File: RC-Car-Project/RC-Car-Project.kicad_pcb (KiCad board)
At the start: 2 copper layers, 80 x 120 mm, 136 parts, among them J1 Conn_01x02_Pin, J10 ANT_IF, J11 Conn_01x02, J12 Conn_01x02, J2 Conn_01x02_Pin, J3 Conn_01x02_Pin, J4 Conn_01x02_Pin, J5 MCU_IF, J6 Conn_01x02, J7 Conn_01x02, J8 Conn_01x02, J9 Conn_02x09_Odd_Even, Q1 BTN8982TA, Q2 BTN8982TA, Q3 BTN8982TA, Q4 2N7002E, Q4 BTN8982TA, Q5 2N7002E, Q6 2N7002E, Q7 PMOS, SW1 SW_Push, U1 LMR16020PDDAR, U10 2450LP14A0100001T, U2 A6986F3V3TR, U3 STM32H743VGTx, U4 AT86RF215-ZU, U5 2450FB15A050E, U6 RFX2401C, U7 INA229AQDGSRQ1, U8 ADC082S021CIMM/NOPB, U9 SN74HC244PWR, Y1 Crystal

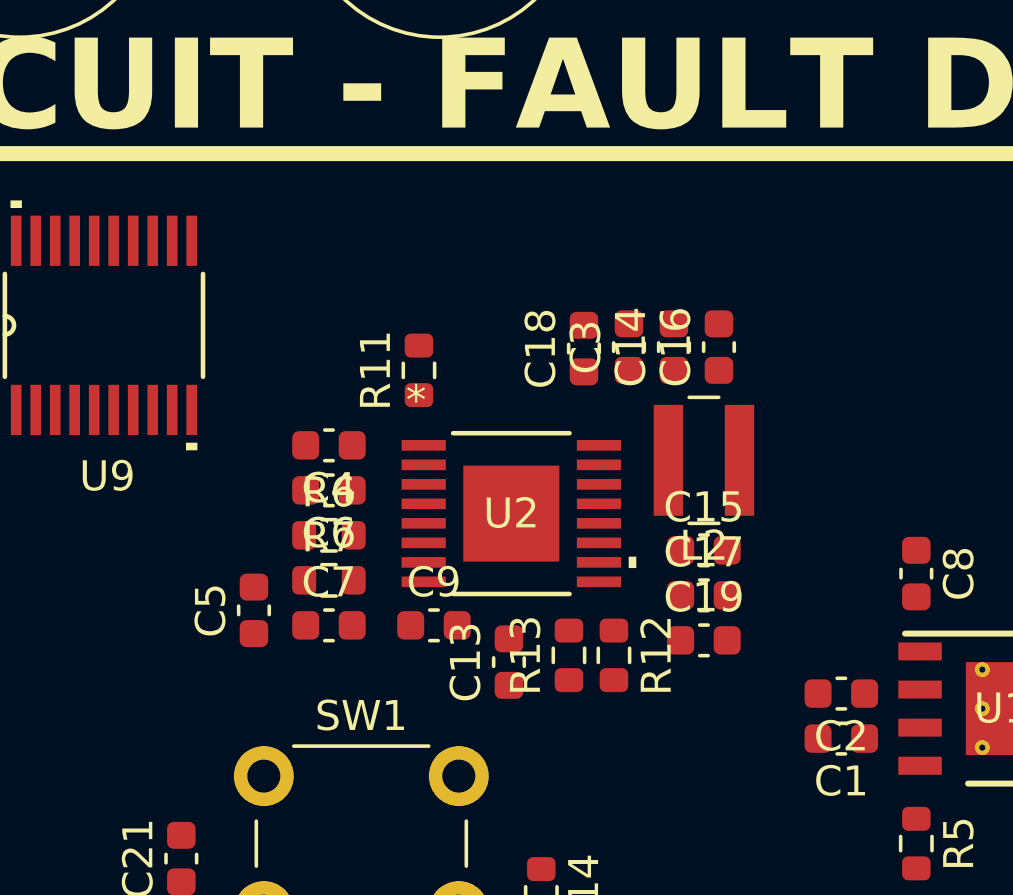
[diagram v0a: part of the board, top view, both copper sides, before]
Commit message: Update DC power supply to 3A and 60V
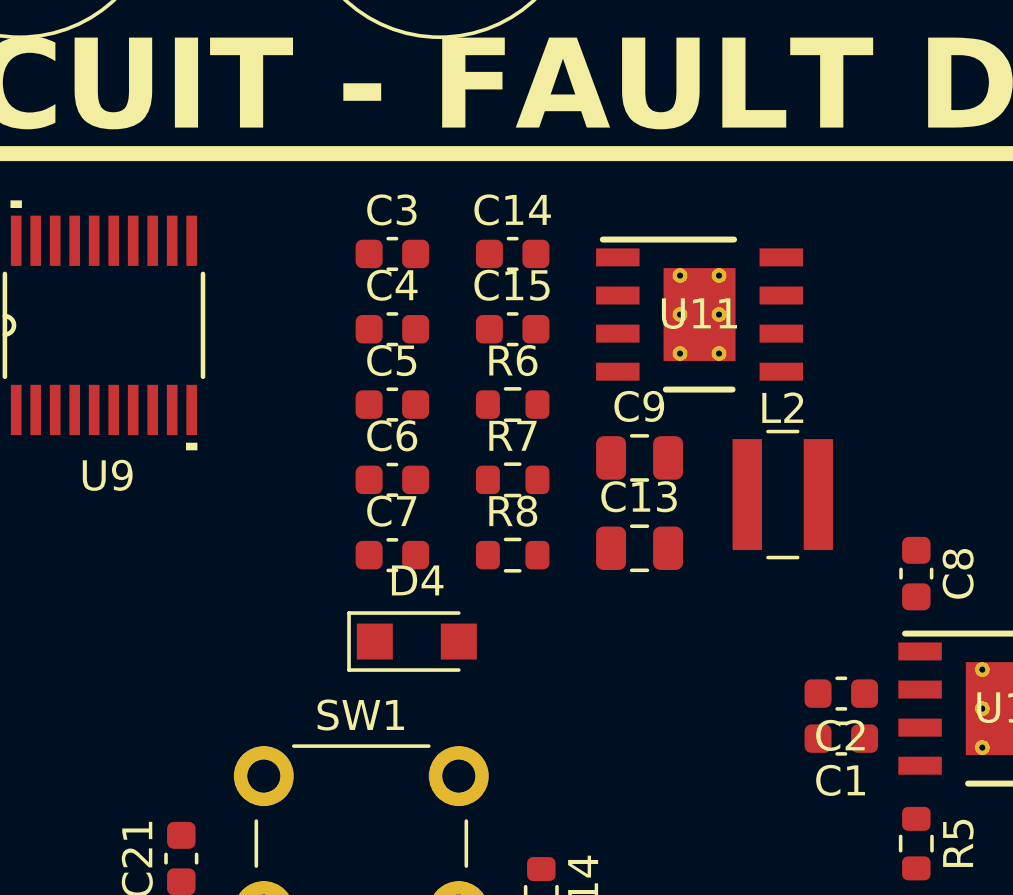
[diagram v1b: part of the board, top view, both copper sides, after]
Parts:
- removed C16, C18: 1uF/50V, Capacitor_SMD:C_0603_1608Metric
- removed C17: 10uF/50V, Capacitor_SMD:C_0603_1608Metric
- removed C19: 1uF/16V, Capacitor_SMD:C_0603_1608Metric
- removed R11: 1Mohm, Resistor_SMD:R_0603_1608Metric
- removed R12: 280kohm, Resistor_SMD:R_0603_1608Metric
- removed R13: 10kohm, Resistor_SMD:R_0603_1608Metric
- removed U2: A6986F3V3TR, footprints:HTSSOP16_4P5X5P1X0P65P_STM
- added D4: D_Schottky, Diode_SMD:Nexperia_CFP3_SOD-123W, F.Cu at (156.9, 104.8)
- added R8: 100kohm, Resistor_SMD:R_0603_1608Metric, F.Cu at (160.0, 101.9)
- added U11: LMR16030PDDA, footprints:DDA0008E_N, F.Cu at (166.3, 93.9)
- C13: value 220pF/16V -> 47uF/16V; footprint Capacitor_SMD:C_0603_1608Metric -> Capacitor_SMD:C_0805_2012Metric
- C14, C15: value 10uF/50V -> 1uF/16V
- C3: value 1uF/50V -> 0.1uF/50V
- C4: value 470nF/25V -> 10uF/50V
- C5: value 220pF/25V -> 1uF/50V
- C6: value 68nF/25V -> 0.1uF/50V
- C7: value 220pF/25V -> 0.1uF/16V
- C9: value 10nF/25V -> 47uF/16V; footprint Capacitor_SMD:C_0603_1608Metric -> Capacitor_SMD:C_0805_2012Metric
- R6: value 1.8kohm -> 40kohm
- R7: value 75kohm -> 340kohm
- R9: value 280kohm -> 150kohm
- moved C15 9.75 mm to (160.0, 94.4)
- moved C9 8.84 mm to (164.3, 98.6)
- moved C3 8.48 mm to (156.0, 91.8), turned to 0 degrees
- moved C5 8.27 mm to (156.0, 96.9), turned to 0 degrees
- moved R6 7.52 mm to (160.0, 96.9)
- moved R7 6.98 mm to (160.0, 99.4)
- moved C14 6.21 mm to (160.0, 91.8), turned to 0 degrees
- moved C13 5.78 mm to (164.3, 101.7), turned to 0 degrees
- moved C4 4.41 mm to (156.0, 94.4), turned to 0 degrees
- moved C7 3.15 mm to (156.0, 101.9)
- moved L2 2.87 mm to (169.1, 99.9), turned to 0 degrees
- moved C6 2.14 mm to (156.0, 99.4), turned to 0 degrees
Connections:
- C13 pad 2: Net-(U2-VOUT) -> GNDA
- C14 pad 1: VDD_BATT -> +3V3
- C36 pad 1: +3V3 -> GNDA
- C36 pad 2: GNDA -> Net-(U4-DVDD)
- C37 pad 1: +3V3 -> GNDA
- C37 pad 2: GNDA -> Net-(U4-AVDD1)
- C38 pad 1: +3V3 -> Net-(U4-AVDD0)
- C4 pad 1: Net-(U2-MLF) -> VDD_BATT
- C5 pad 1: GNDA -> VDD_BATT
- C5 pad 2: Net-(C5-Pad2) -> GNDA
- C6 pad 1: Net-(U2-SS/*INH) -> VDD_BATT
- C7 pad 1: GNDA -> Net-(D4-K)
- C7 pad 2: Net-(U2-COMP) -> Net-(U11-BOOT)
- C9 pad 1: Net-(U2-DELAY) -> +3V3
- J1 pad 2: VDD_BATT -> VDD_BATT_PRE_SW
- J2 pad 2: VDD_BATT -> VDD_BATT_PRE_SW
- L2 pad 1: Net-(L2-Pad1) -> Net-(D4-K)
- R6 pad 1: GNDA -> Net-(U11-RT_SYNC)
- R6 pad 2: Net-(U2-FSW) -> GNDA
- R7 pad 1: Net-(C5-Pad2) -> Net-(U11-FB)
- R7 pad 2: Net-(U2-COMP) -> +3V3
- U4 pad 14: +3V3 -> Net-(U4-AVDD0)
- U4 pad 37: +3V3 -> Net-(U4-DVDD)
- U4 pad 47: +3V3 -> Net-(U4-AVDD1)

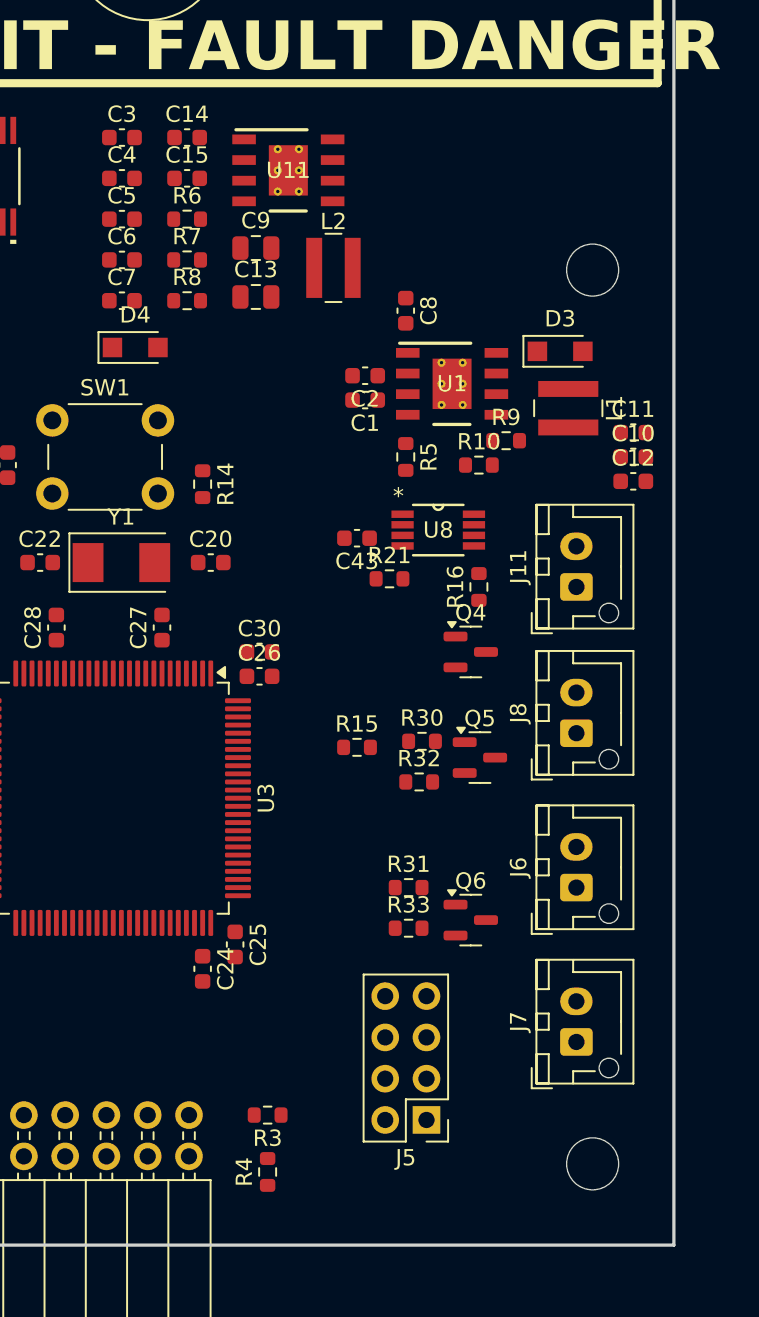
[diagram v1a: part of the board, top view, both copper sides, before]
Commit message: Fix power supply layout
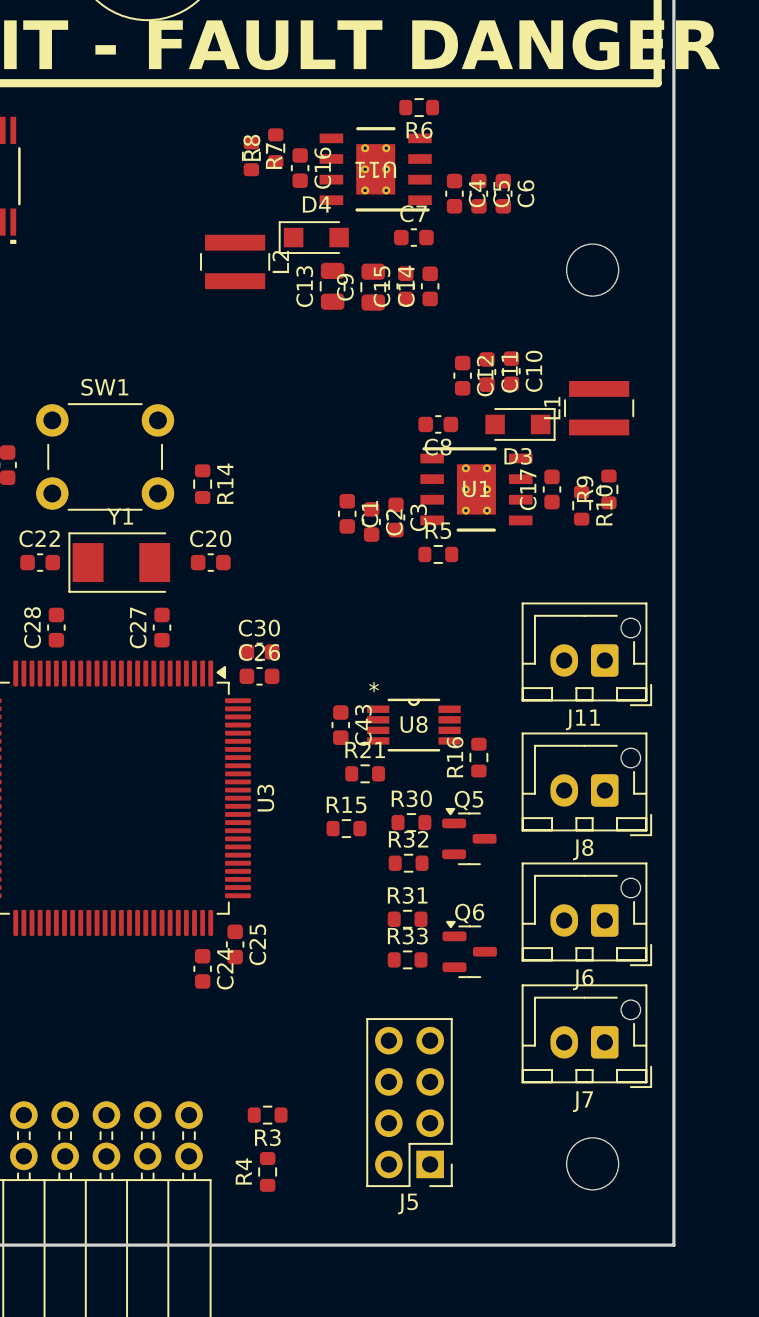
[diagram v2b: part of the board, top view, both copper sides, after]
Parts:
- removed the Q4 at (177.5, 123.5)
- added C16: 0.1uF/50V, Capacitor_SMD:C_0603_1608Metric, F.Cu at (167.0, 93.7)
- added C17: 0.1uF/50V, Capacitor_SMD:C_0603_1608Metric, F.Cu at (182.5, 113.5)
- moved C3 28.8 mm to (172.9, 115.2), turned to -90 degrees
- moved C6 23.8 mm to (179.5, 95.3), turned to -90 degrees
- moved C5 22.0 mm to (178.0, 95.3), turned to -90 degrees
- moved C4 20.5 mm to (176.5, 95.3), turned to -90 degrees
- moved C7 18.4 mm to (174.0, 98.0)
- moved C14 17.5 mm to (175.0, 101.0), turned to 90 degrees
- moved R6 15.8 mm to (174.3, 90.0), turned to 180 degrees
- moved C15 15.0 mm to (173.5, 101.0), turned to 90 degrees
- moved D4 13.0 mm to (168.0, 98.0)
- moved C12 12.3 mm to (177.0, 106.5), turned to -90 degrees
- moved R21 12.1 mm to (171.0, 131.0)
- moved U8 12.1 mm to (174.0, 128.0)
- moved C43 11.5 mm to (169.5, 128.0), turned to -90 degrees
- moved R8 10.9 mm to (165.5, 92.5), turned to 90 degrees
- moved R16 10.5 mm to (178.0, 130.0)
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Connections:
- U1 pad 6: unconnected-(U1-PWRGD-Pad6) -> Net-(U1-PWRGD)
- U11 pad 6: unconnected-(U11-PWRGD-Pad6) -> Net-(U11-PWRGD)

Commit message: I'm tired boss
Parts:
- removed C36, C37, C38, C39, C40: 0.1uF/10V, Capacitor_SMD:C_0603_1608Metric
- removed C49: 0.3pF, Capacitor_SMD:C_0603_1608Metric
- removed C50, C51, C52, C53: 1.5pF, Capacitor_SMD:C_0603_1608Metric
- removed L3, L4: 2.4nH, Inductor_SMD:L_0603_1608Metric
- removed the R19 at (134.8, 97.0)
- removed the R20 at (134.7, 98.5)
- removed REF** (x6): MountingHole_3.2mm_M3, MountingHole:MountingHole_3.2mm_M3
- removed U10: 2450LP14A0100001T, footprints:ICCAF50P160X80X70-6N
- removed U5: 2450FB15A050E, footprints:2450FB15A050E_JOT
- removed U6: RFX2401C, footprints:RFX2401C_SKY
- added C18: 10uF/10V, Capacitor_SMD:C_0603_1608Metric, F.Cu at (46.3, 104.2)
- added C19: 100nF/10V, Capacitor_SMD:C_0603_1608Metric, F.Cu at (46.3, 106.7)
- added D8: PMEG060V100EPD, Package_TO_SOT_SMD:Nexperia_CFP15_SOT-1289, F.Cu at (70.6, 121.9)
- added D9: PMEG060V100EPD, Package_TO_SOT_SMD:Nexperia_CFP15_SOT-1289, F.Cu at (70.6, 127.9)
- added FB1: FerriteBead, Capacitor_SMD:C_0603_1608Metric, F.Cu at (50.3, 106.7)
- added J13: RF_IF, Connector_PinHeader_2.54mm:PinHeader_2x04_P2.54mm_Vertical, F.Cu at (68.7, 105.3)
- added J15: USB4120-03-C_REVA, USB4120-03-C:GCT_USB4120-03-C_REVA, F.Cu at (81.7, 106.3)
- added R11: 10k, Capacitor_SMD:C_0603_1608Metric, F.Cu at (50.3, 109.2)
- added R12: 10k, Capacitor_SMD:C_0603_1608Metric, F.Cu at (50.3, 111.8)
- added R13: 10k, Capacitor_SMD:C_0603_1608Metric, F.Cu at (50.3, 114.3)
- added R34: 10k, Capacitor_SMD:C_0603_1608Metric, F.Cu at (50.3, 116.8)
- added R35: 10k, Capacitor_SMD:C_0603_1608Metric, F.Cu at (54.3, 104.2)
- added R36: 10k, Capacitor_SMD:C_0603_1608Metric, F.Cu at (54.3, 106.7)
- added R37: 10k, Capacitor_SMD:C_0603_1608Metric, F.Cu at (54.3, 109.2)
- added R38: 10k, Capacitor_SMD:C_0603_1608Metric, F.Cu at (54.3, 111.8)
- added R39: 10k, Capacitor_SMD:C_0603_1608Metric, F.Cu at (54.3, 114.3)
- added R40: 10k, Capacitor_SMD:C_0603_1608Metric, F.Cu at (54.3, 116.8)
- added R41: 10k, Capacitor_SMD:C_0603_1608Metric, F.Cu at (58.3, 104.2)
- added R42: 10k, Capacitor_SMD:C_0603_1608Metric, F.Cu at (58.3, 106.7)
- added R43: 10k, Capacitor_SMD:C_0603_1608Metric, F.Cu at (58.3, 109.2)
- added R44: 10k, Capacitor_SMD:C_0603_1608Metric, F.Cu at (58.3, 111.8)
- added R45: 10k, Capacitor_SMD:C_0603_1608Metric, F.Cu at (58.3, 114.3)
- added R46: 0ohm, Resistor_SMD:R_0603_1608Metric, F.Cu at (58.3, 116.8)
- added R47: 10k, Capacitor_SMD:C_0603_1608Metric, F.Cu at (62.4, 104.2)
- added R48: 10k, Capacitor_SMD:C_0603_1608Metric, F.Cu at (62.4, 106.7)
- added R49: 10k, Capacitor_SMD:C_0603_1608Metric, F.Cu at (62.4, 109.2)
- added R50: 10k, Capacitor_SMD:C_0603_1608Metric, F.Cu at (62.4, 111.8)
- added R51: 10k, Capacitor_SMD:C_0603_1608Metric, F.Cu at (62.4, 114.3)
- added R52: 10k, Capacitor_SMD:C_0603_1608Metric, F.Cu at (62.4, 116.8)
- added R53: 5.11kohm, Resistor_SMD:R_0603_1608Metric, F.Cu at (80.7, 113.1)
- added R54: 5.11kohm, Resistor_SMD:R_0603_1608Metric, F.Cu at (80.7, 115.6)
- added TP1: TestPoint, Connector_PinHeader_2.54mm:PinHeader_1x02_P2.54mm_Vertical, F.Cu at (77.2, 121.2)
- added U2: ~, FGH100M:FGH100MABMD, F.Cu at (177.0, 139.3)
- C31, C35: value 0.1uF/10V -> 100nF/10V
- C32, C34: value 0.1uF/10V -> DNP
- C33: value 0.1uF/10V -> 10uF/10V
- U4: value AT86RF215-ZU -> USBLC6-2SC6; footprint footprints:QFN48_PQ_MCH -> Package_TO_SOT_SMD:SOT-23-6
- moved C34 91.3 mm to (46.3, 116.8)
- moved C35 89.3 mm to (50.3, 104.2)
- moved C33 80.3 mm to (46.3, 114.3), turned to 0 degrees
- moved C31 79.8 mm to (46.3, 109.2), turned to 0 degrees
- moved C32 79.6 mm to (46.3, 111.8), turned to 0 degrees
- moved C21 74.1 mm to (222.7, 119.8), turned to 0 degrees
- moved R14 63.3 mm to (221.5, 131.8), turned to 180 degrees
- moved U4 56.4 mm to (76.1, 114.3), turned to 0 degrees
- moved J10 53.4 mm to (182.4, 155.4)
- moved C10 53.1 mm to (233.1, 104.7)
- moved C11 53.1 mm to (231.6, 104.8)
- moved C12 53.1 mm to (230.1, 105.0)
- moved C13 53.1 mm to (222.1, 99.5)
- moved C14 53.1 mm to (228.1, 99.5)
- moved C15 53.1 mm to (226.6, 99.5)
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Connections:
- C32 pad 1: +3V3 -> Net-(U2-ANT_WIFI)
- C33 pad 1: +3V3 -> VDD_FEM
- C34 pad 1: +3V3 -> /Connectors/RF_ANT
- C35 pad 1: +3V3 -> VDD_FEM
- C4 pad 1: VDD_BATT -> Net-(D8-K)
- C5 pad 1: VDD_BATT -> Net-(D8-K)
- C6 pad 1: VDD_BATT -> Net-(D8-K)
- U11 pad 2: VDD_BATT -> Net-(D8-K)
- U11 pad 3: VDD_BATT -> Net-(D8-K)
- U3 pad 18: /IVTSense/INA_CS -> unconnected-(U3-PC3_C-Pad18)
- U3 pad 32: /IVTSense/THERMO_ADC_CS -> unconnected-(U3-PC4-Pad32)
- U3 pad 40: /MCU/RF_NRST -> unconnected-(U3-PE10-Pad40)
- U3 pad 41: /MCU/SPI4_CS_RF -> unconnected-(U3-PE11-Pad41)
- U3 pad 42: /MCU/SPI4_SCLK_RF -> unconnected-(U3-PE12-Pad42)
- U3 pad 43: /MCU/SPI4_MISO_RF -> unconnected-(U3-PE13-Pad43)
- U3 pad 5: /MCU/SPI4_MOSI_RF -> /Connectors/DCMI_D7
- U3 pad 65: /Connectors/DCMI_D2 -> /MCU/SDMMC1_D0
- U3 pad 66: /Connectors/DCMI_D3 -> /MCU/SDMMC1_D1
- U3 pad 70: unconnected-(U3-PA11-Pad70) -> /Connectors/CON_USB_D-
- U3 pad 71: unconnected-(U3-PA12-Pad71) -> /Connectors/CON_USB_D+
- U3 pad 78: unconnected-(U3-PC10-Pad78) -> /MCU/SDMMC1_D2
- U3 pad 79: unconnected-(U3-PC11-Pad79) -> /MCU/SDMMC1_D3
- U3 pad 8: unconnected-(U3-PC14-Pad8) -> /IVTSense/THERMO_ADC_CS
- U3 pad 80: unconnected-(U3-PC12-Pad80) -> /MCU/SDMMC1_CK
- U3 pad 81: unconnected-(U3-PD0-Pad81) -> /MCU/RF_RESET
- U3 pad 83: unconnected-(U3-PD2-Pad83) -> /MCU/SDMMC1_CMD
- U3 pad 9: unconnected-(U3-PC15-Pad9) -> /IVTSense/INA_CS
- U3 pad 96: /Connectors/DCMI_D7 -> unconnected-(U3-PB9-Pad96)
- U3 pad 97: unconnected-(U3-PE0-Pad97) -> /Connectors/DCMI_D2
- U3 pad 98: unconnected-(U3-PE1-Pad98) -> /Connectors/DCMI_D3
- U4 pad 1: /RF/RXEN -> Net-(J15-D1-)
- U4 pad 2: /RF/TXEN -> GNDA
- U4 pad 3: GNDA -> Net-(J15-D1+)
- U4 pad 4: Net-(U4-RFP24) -> /Connectors/CON_USB_D+
- U4 pad 5: Net-(U4-RFN24) -> VDD_USB
- U4 pad 6: GNDA -> /Connectors/CON_USB_D-
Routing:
- net /Connectors/DCMI_VSYNC: track 0.00 -> 35.9 mm, vias 0 -> 2
- net /Connectors/DCMI_D3: track 0.00 -> 32.6 mm, vias 0 -> 1
- net /Connectors/DCMI_D7: track 0.00 -> 31.6 mm, vias 0 -> 1
- net /Connectors/DCMI_D4: track 0.00 -> 30.4 mm, vias 0 -> 1
- net /Connectors/DCMI_D6: track 0.00 -> 29.0 mm, vias 0 -> 1
- net /Connectors/DCMI_PIXCLK: track 0.00 -> 28.9 mm, vias 0 -> 1
- net /Connectors/DCMI_D2: track 0.00 -> 28.0 mm, vias 0 -> 1
- net /Connectors/DCMI_XCLK: track 0.00 -> 25.6 mm, vias 0 -> 1
- net /Connectors/DCMI_HSYNC: track 0.00 -> 25.1 mm, vias 0 -> 1
- net /Connectors/DCMI_D5: track 0.00 -> 21.8 mm
- net /Connectors/I2C2_CAM_SCL: track 0.00 -> 18.6 mm
- net /Connectors/I2C2_CAM_SDA: track 0.00 -> 15.2 mm
- net /Connectors/DCMI_D1: track 0.00 -> 13.9 mm
- net /Connectors/DCMI_D0: track 0.00 -> 9.96 mm
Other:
- copper layers 2 -> 4
